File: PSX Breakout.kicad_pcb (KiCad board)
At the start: 2 copper layers, 100 x 51.8 mm, 28 parts, among them J1 Conn_01x12_Male, J2 Mini-DIN-4, J3 VAL**, J4 DB15_Female_HighDensity, J5 3x2_RCA, SW1 SW_SPDT, SW2 SW_SP3T, SW3 SW_SP3T, U1 LM1881

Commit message: Update PSX Breakout.kicad_pcb
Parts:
- added BTM: Case_BTM, PSX_BREAKOUT:Case_BTM, F.Cu at (140.0, 94.0)
- added TOP: Case_TOP, PSX_BREAKOUT:Case_TOP, F.Cu at (140.0, 94.0)
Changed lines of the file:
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@@
-(kicad_pcb (version 20171130) (host pcbnew "(5.1.0)-1")
+(kicad_pcb (version 20171130) (host pcbnew "(5.1.2)-1")
   (general
     (thickness 1.6)
@@
     (tracks 289)
     (zones 0)
-    (modules 28)
+    (modules 30)
     (nets 32)
   )
@@
     (add_net VGA_SYNC_OUT)
   )
+  (module PSX_BREAKOUT:Case_BTM (layer F.Cu)
+    (at 140 93.98)
+    (fp_text reference BTM (at 0.0762 2.0066) (layer F.SilkS) hide
+      (effects (font (size 1 1) (thickness 0.15)))
+    )
+    (fp_text value Case_BTM (at 0 -1.7272) (layer F.Fab)
+      (effects (font (size 1 1) (thickness 0.15)))
+    )
+    (fp_circle (center 0 0) (end 0 0.0254) (layer Dwgs.User) (width 0.12))
+    (model ${KIPRJMOD}/PSX_BREAKOUT.Pretty/Case_BTM.step
+      (offset (xyz 0 0 -5.84))
+      (scale (xyz 1 1 1))
+      (rotate (xyz 0 0 0))
+    )
+  )
+  (module PSX_BREAKOUT:Case_TOP (layer F.Cu)
+    (at 140 93.98)
+    (fp_text reference TOP (at 0.0762 2.0066) (layer F.SilkS) hide
+      (effects (font (size 1 1) (thickness 0.15)))
+    )
+    (fp_text value Case_TOP (at 0 -1.7272) (layer F.Fab)
+      (effects (font (size 1 1) (thickness 0.15)))
+    )
+    (fp_circle (center 0 0) (end 0 0.0254) (layer Dwgs.User) (width 0.12))
+    (model ${KIPRJMOD}/PSX_BREAKOUT.Pretty/Case_TOP.step
+      (offset (xyz 0 0 12))
+      (scale (xyz 1 1 1))
+      (rotate (xyz 0 0 0))
+    )
+  )
   (module Connector_Dsub:DSUB-15-HD_Female_Horizontal_P2.29x1.98mm_EdgePinOffset3.03mm_Housed_MountingHolesOffset4.94mm (layer F.Cu)

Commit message: Fixing Merging Error
Updated Case, moved connector, generated gerbers
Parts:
- removed BTM: Case_BTM, PSX_BREAKOUT:Case_BTM
- removed the REF** at (98.5, 98.3)
- removed the REF** at (118.4, 80.1)
- removed the REF** at (161.5, 80.4)
- removed the REF** at (178.0, 87.5)
- removed TOP: Case_TOP, PSX_BREAKOUT:Case_TOP
- added REF**: MountingHole_3.2mm_M3, MountingHole:MountingHole_3.2mm_M3, F.Cu at (109.7, 96.6)
- added REF**: MountingHole_3.2mm_M3, MountingHole:MountingHole_3.2mm_M3, F.Cu at (107.4, 81.4)
- added REF**: MountingHole_3.2mm_M3, MountingHole:MountingHole_3.2mm_M3, F.Cu at (162.2, 92.3)
- added REF**: MountingHole_3.2mm_M3, MountingHole:MountingHole_3.2mm_M3, F.Cu at (146.3, 81.2)
- moved FB1 42.4 mm to (186.1, 65.5)
- moved J1 42.4 mm to (182.4, 60.0)
- moved C3 27.8 mm to (178.9, 83.1)
- moved JP3 27.8 mm to (182.2, 83.1)
- moved JP4 27.8 mm to (160.0, 83.1)
- moved C2 27.8 mm to (167.8, 83.1)
- moved C4 27.8 mm to (156.7, 83.1)
- moved JP2 27.8 mm to (171.2, 83.1)
- moved C5 24.8 mm to (129.4, 90.4), turned to 270 degrees
- moved C8 20.9 mm to (134.4, 87.2)
- moved R2 20.9 mm to (134.4, 85.5)
- moved C1 20.3 mm to (114.8, 87.5)
- moved R1 16.9 mm to (124.6, 83.2)
- moved JP1 15.4 mm to (120.5, 78.1)
- moved C6 14.8 mm to (121.2, 91.7)
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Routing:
- net GND: track 87.3 -> 22.9 mm, vias 35 -> 20
- net GREEN_OUT: track 68.5 -> 115.6 mm, vias 2 -> 1
- net CHROMA: track 41.7 -> 87.5 mm, vias 1 -> 2
- net CSYNC: track 138.3 -> 109.6 mm, vias 1 -> 2
- net RED_OUT: track 95.7 -> 117.2 mm, vias 4 -> 3
- net RED: track 25.5 -> 46.2 mm
- net Net-(C1-Pad2): track 5.13 -> 24.2 mm
- net LUMA: track 166.9 -> 148.5 mm
- net BLUE: track 31.3 -> 47.4 mm
- net Net-(C5-Pad1): track 72.9 -> 85.0 mm
- net Net-(C1-Pad1): track 14.5 -> 2.77 mm, vias 2 -> 0
- net RIGHT: track 115.4 -> 104.4 mm, vias 0 -> 2
- net Net-(C8-Pad1): track 5.90 -> 13.5 mm
- net BLUE_OUT: track 89.3 -> 95.5 mm, vias 2 -> 0
- net CVBS: track 150.4 -> 146.4 mm
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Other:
- outline, holes or cut-outs redrawn

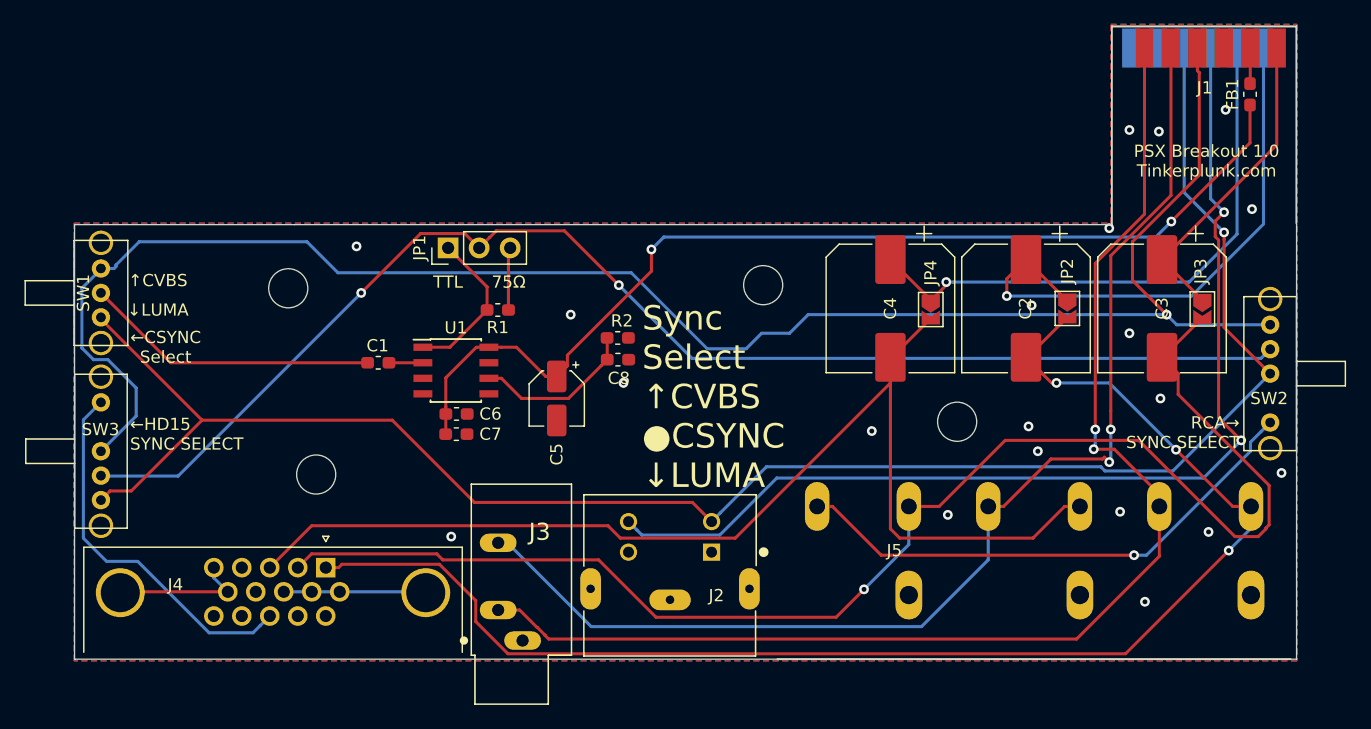
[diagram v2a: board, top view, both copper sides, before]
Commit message: Changed headphone jack footprint
Added pins to the headphone jack footprint so it is compatible with all SJ1-353x-n, ng, and ns series jacks.
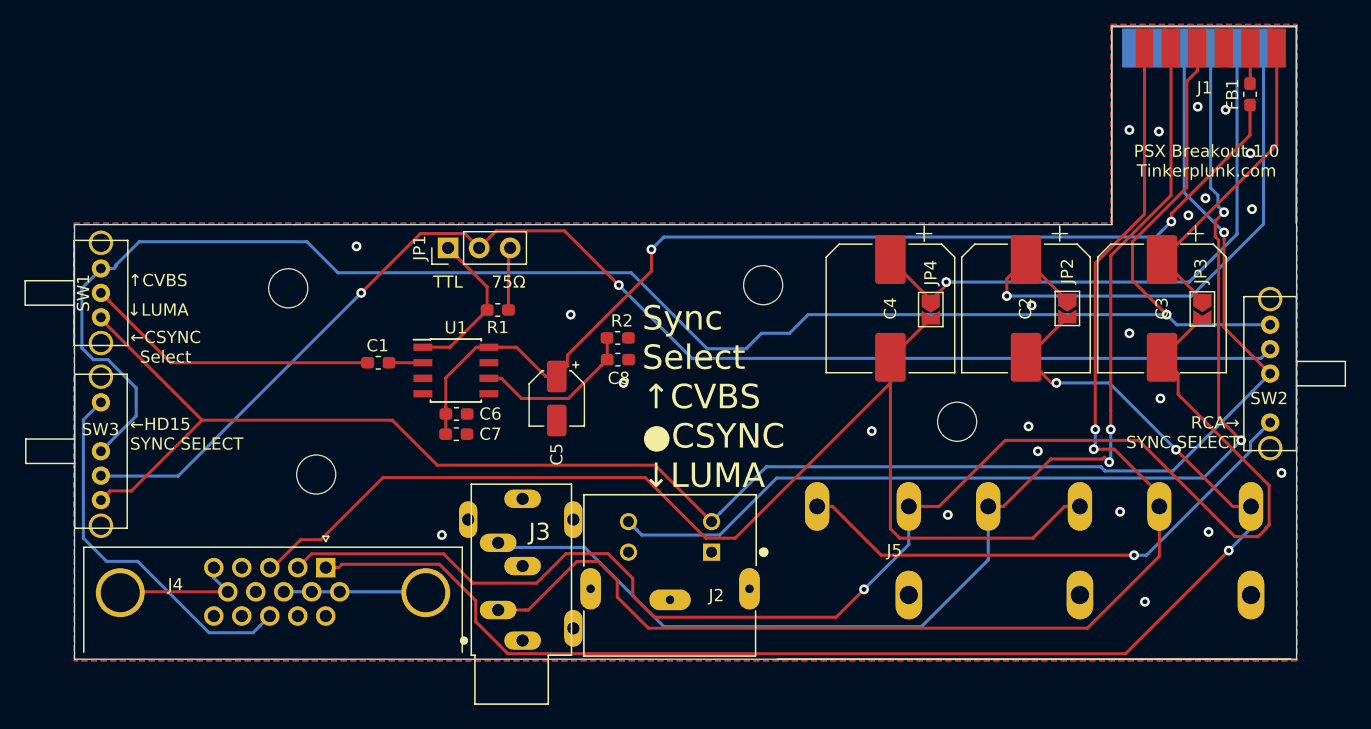
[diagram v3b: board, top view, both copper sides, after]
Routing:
- net RIGHT: track 104.4 -> 107.8 mm
- net BLUE_OUT: track 95.5 -> 98.8 mm
- net GREEN_OUT: track 115.6 -> 118.4 mm
- net GND: vias 20 -> 23

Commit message: Completed BOM
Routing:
- net GND: vias 23 -> 22
- net (no net): vias 0 -> 1
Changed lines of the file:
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@@
   (segment (start 101.3505 105.102) (end 102.4955 106.247) (width 0.25) (layer B.Cu) (net 10))
   (segment (start 101.3505 104.267) (end 101.3505 105.102) (width 0.25) (layer B.Cu) (net 10))
-  (via (at 120.015 101.6) (size 0.8) (drill 0.4) (layers F.Cu B.Cu) (net 10))
+  (via (at 120.015 101.6) (size 0.8) (drill 0.4) (layers F.Cu B.Cu) (net 0))
   (via (at 186.182 70.358) (size 0.8) (drill 0.4) (layers F.Cu B.Cu) (net 10))
   (via (at 182.499 74.041) (size 0.8) (drill 0.4) (layers F.Cu B.Cu) (net 10))

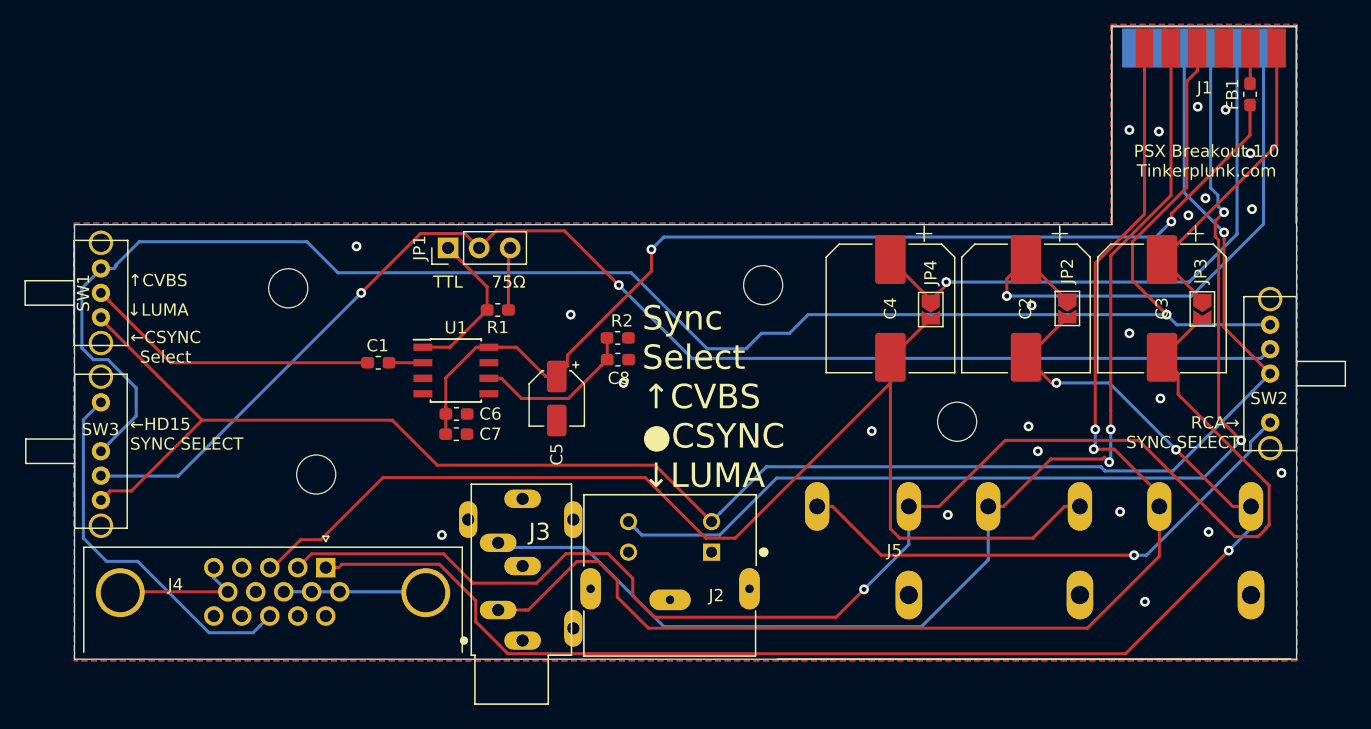
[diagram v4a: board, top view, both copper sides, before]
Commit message: Big Changes
Moved the csync selector switch to the right in order to move the hd15 connector back to the right position. Fixed hd15 footprint, moved screw holes and updated case with new screw holes and input labels. Updated 3d model for HD15 connector.
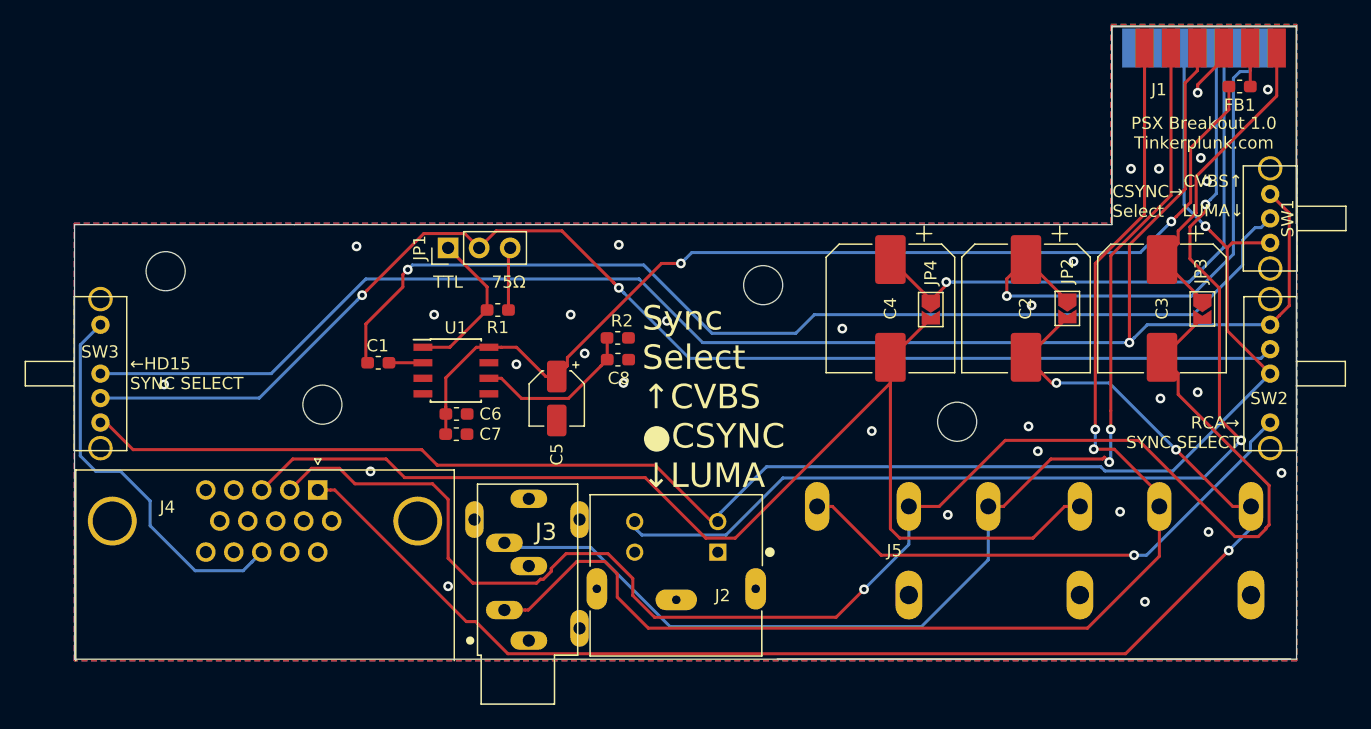
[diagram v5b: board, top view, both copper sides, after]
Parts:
- J4: footprint Connector_Dsub:DSUB-15-HD_Female_Horizontal_P2.29x1.98mm_EdgePinOffset3.03mm_Housed_MountingHolesOffset4.94mm -> Connector_Dsub:DSUB-15-HD_Female_Horizontal_P2.29x1.98mm_EdgePinOffset8.35mm_Housed_MountingHolesOffset10.89mm
- moved SW1 95.9 mm to (187.8, 75.7), turned to 90 degrees
- moved REF** 10.1 mm to (97.4, 80.0)
- moved J4 6.38 mm to (109.9, 97.9)
- moved SW3 6.35 mm to (92.1, 88.4)
- moved REF** 5.74 mm to (110.2, 90.9)
- moved FB1 1.06 mm to (185.3, 64.9), turned to 0 degrees
- moved J2 0.51 mm to (139.2, 104.9)
- moved J3 0.51 mm to (127.1, 110.2)
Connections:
- SW1 pad 1: CVBS -> LUMA
- SW1 pad 3: LUMA -> CVBS
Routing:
- net Net-(C1-Pad2): track 24.2 -> 87.2 mm, vias 0 -> 1
- net GND: track 22.9 -> 4.54 mm, vias 22 -> 30
- net LUMA: track 148.5 -> 137.6 mm
- net GREEN_OUT: track 118.4 -> 125.2 mm
- net CVBS: track 146.3 -> 140.1 mm
- net CSYNC: track 109.6 -> 107.0 mm
- net RED_OUT: track 117.2 -> 119.3 mm
- net VGA_SYNC_OUT: track 30.7 -> 32.0 mm
- net CHROMA: track 87.5 -> 88.7 mm
- net BLUE_OUT: track 98.8 -> 98.1 mm
- net (no net): vias 1 -> 0
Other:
- board text added: "CSYNC→ Select"
- board text added: "CVBS↑"
- board text added: "LUMA↓"
- board text removed: "←CSYNC Select"
- board text removed: "↑CVBS"
- board text removed: "↓LUMA"
